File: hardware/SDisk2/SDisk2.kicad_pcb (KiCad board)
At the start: 2 copper layers, 29 parts, among them J1 SD_Card, J2 To Apple II DISK controller, SW1 BTN_UP, SW2 BTN_ENTER, SW3 BTN_DOWN, U1 74LS125, U2 ATmega328P-PU, U3 LM317_SOT-223, Y1 25Mhz

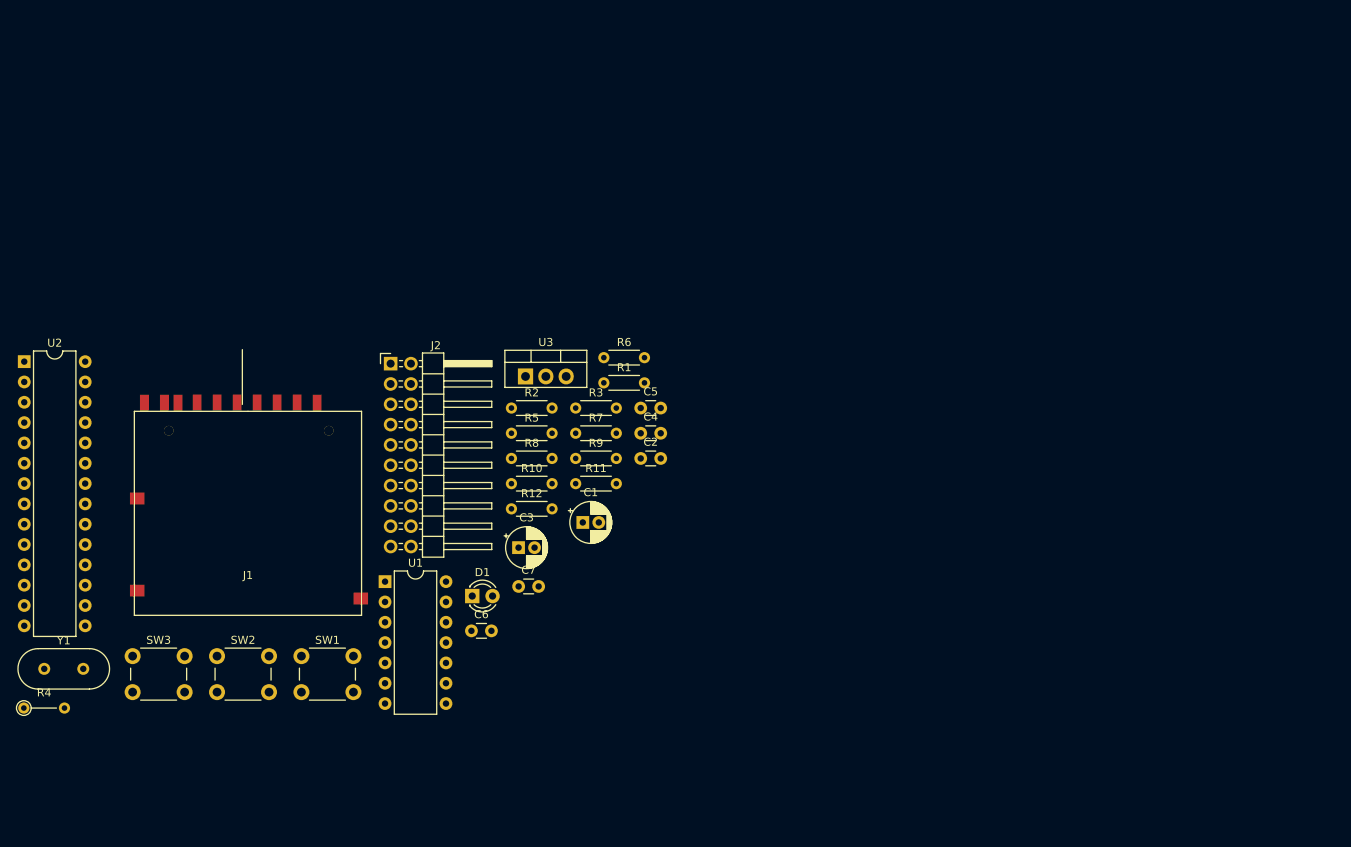
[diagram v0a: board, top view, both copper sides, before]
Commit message: Create netlist and begin place and route
Signed-off-by: Rangel Ivanov <rangelivanov88@gmail.com>
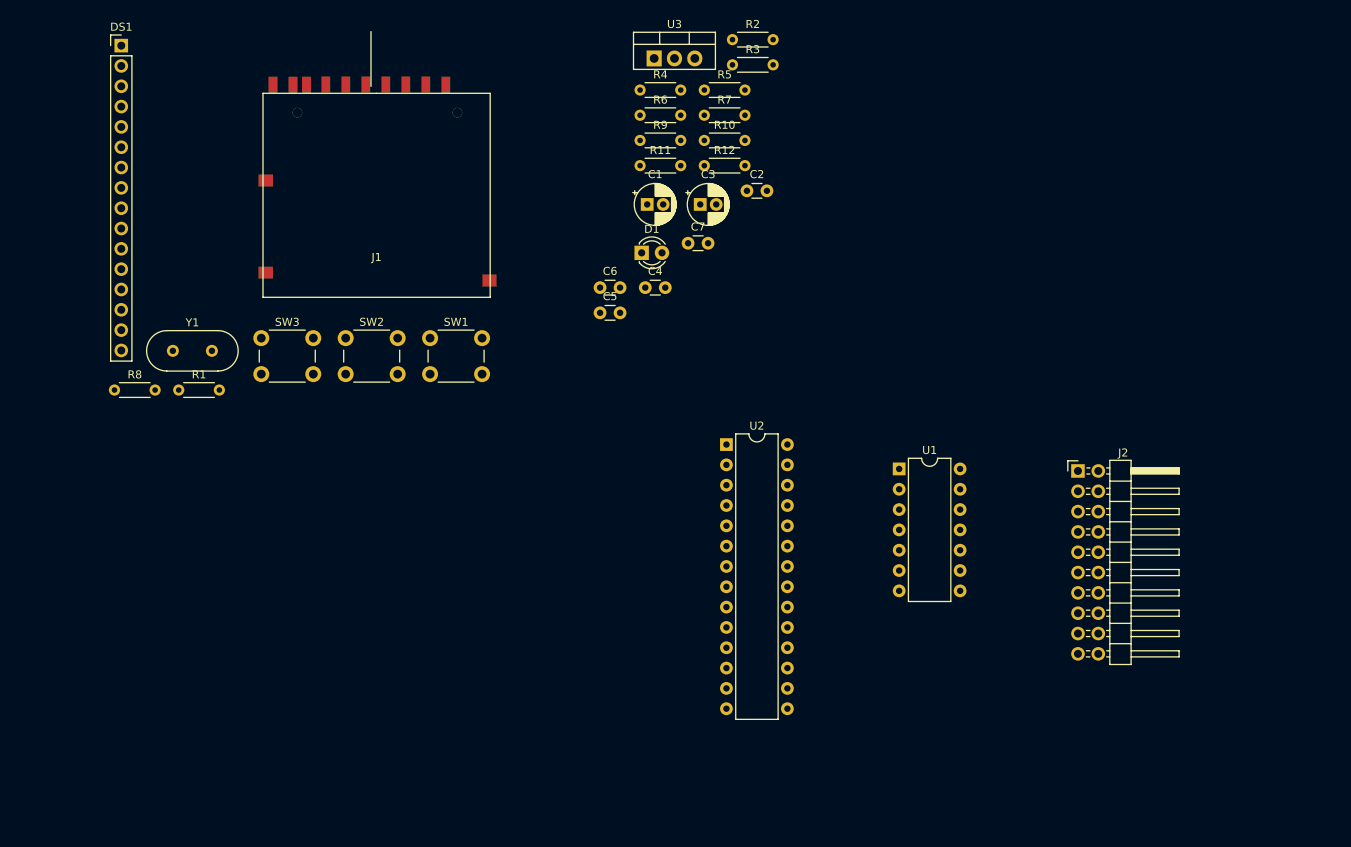
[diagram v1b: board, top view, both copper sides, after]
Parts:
- added DS1: WH1602B-TMI-CT#, Connector_PinHeader_2.54mm:PinHeader_1x16_P2.54mm_Vertical, F.Cu at (50.3, 41.1)
- R4: footprint Resistor_THT:R_Axial_DIN0204_L3.6mm_D1.6mm_P5.08mm_Vertical -> Resistor_THT:R_Axial_DIN0204_L3.6mm_D1.6mm_P5.08mm_Horizontal
- moved R4 109.1 mm to (115.2, 46.6)
- moved U2 88.4 mm to (126.0, 90.9)
- moved J2 87.0 mm to (169.9, 94.2)
- moved U1 65.8 mm to (147.6, 94.0)
- moved R2 53.7 mm to (126.7, 40.3)
- moved R1 53.1 mm to (57.5, 84.1)
- moved R8 50.4 mm to (49.5, 84.1)
- moved R10 49.2 mm to (123.2, 52.9)
- moved R12 49.2 mm to (123.2, 56.1)
- moved R5 49.2 mm to (123.2, 46.6)
- moved C3 48.5 mm to (122.7, 60.9)
- moved C7 47.8 mm to (121.2, 65.8)
- moved D1 47.8 mm to (115.4, 67.0)
- moved R3 47.2 mm to (126.7, 43.5)
- moved C6 45.8 mm to (110.2, 71.3)
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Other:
- net class Default: clearance 0.2 -> 0.22
- rule trace_clearance: 0.2 -> 0.22

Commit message: Initial PCB place and route
Signed-off-by: Rangel Ivanov <rangelivanov88@gmail.com>
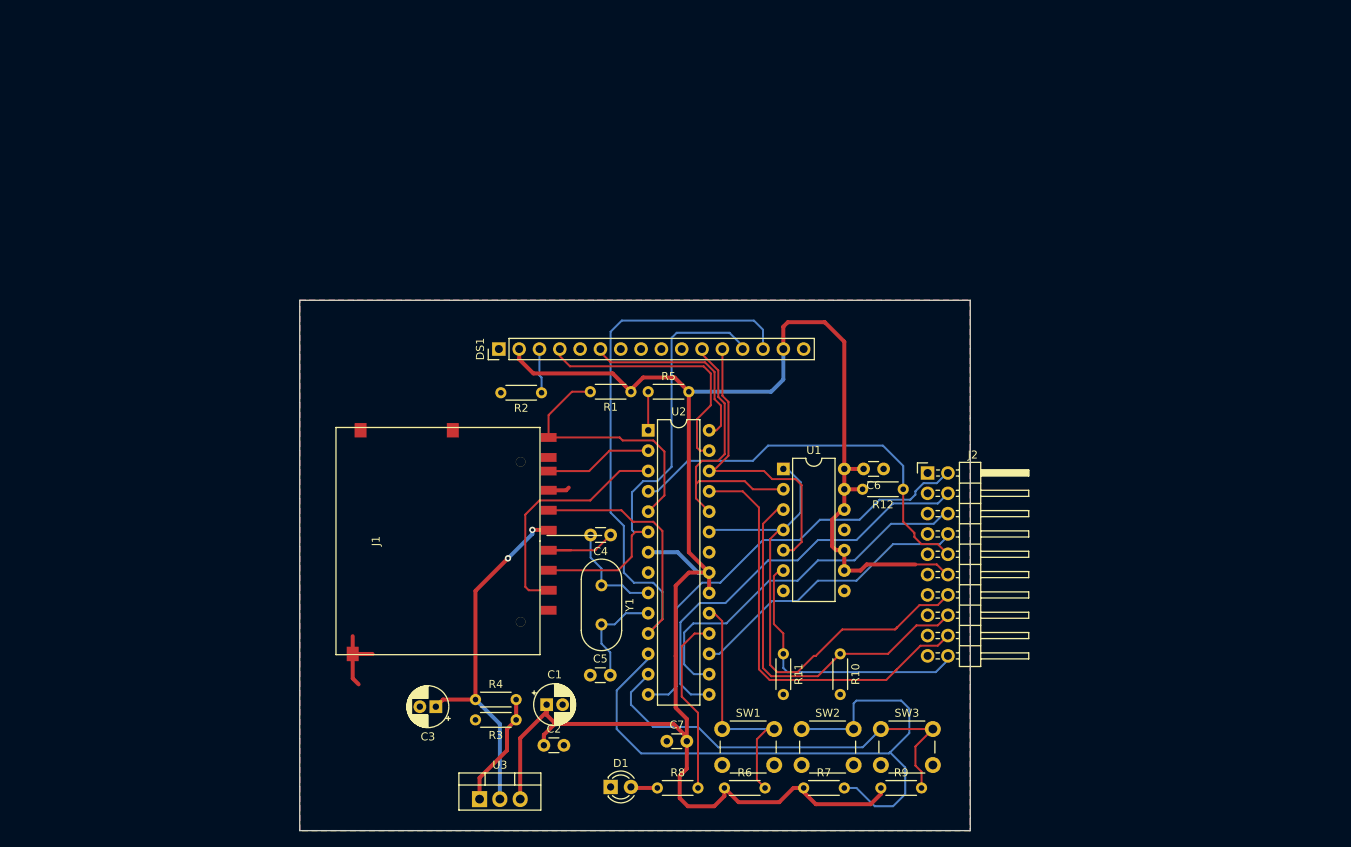
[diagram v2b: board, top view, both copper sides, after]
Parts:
- moved U3 95.1 mm to (95.1, 135.3)
- moved SW3 91.6 mm to (145.3, 126.5)
- moved R9 86.4 mm to (145.3, 133.9)
- moved R3 86.2 mm to (99.7, 125.3), turned to 180 degrees
- moved R7 85.0 mm to (135.6, 133.9)
- moved R6 84.7 mm to (125.7, 133.9)
- moved R8 84.1 mm to (117.3, 133.9)
- moved R4 78.9 mm to (94.6, 122.8)
- moved SW2 75.1 mm to (135.4, 126.5)
- moved C2 73.8 mm to (103.2, 128.5)
- moved C3 70.9 mm to (89.7, 123.7), turned to 180 degrees
- moved D1 66.9 mm to (111.5, 133.7)
- moved R10 66.4 mm to (140.2, 117.1), turned to 270 degrees
- moved C1 63.8 mm to (103.5, 123.4)
- moved R11 63.6 mm to (133.1, 117.1), turned to 270 degrees
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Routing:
- net +5V: track 0.00 -> 238.2 mm
- net /SD_CLK: track 0.00 -> 93.9 mm
- net /BTN_ENTER: track 0.00 -> 85.4 mm
- net /DRIVE_EN: track 0.00 -> 63.7 mm
- net /SD_DI: track 0.00 -> 55.5 mm
- net /STEP0: track 0.00 -> 54.9 mm
- net /BTN_DOWN: track 0.00 -> 54.2 mm
- net /WRITE: track 0.00 -> 54.0 mm
- net /STEP1: track 0.00 -> 52.0 mm
- net /W_REQUEST: track 0.00 -> 49.9 mm
- net /RD_PULSE: track 0.00 -> 48.4 mm
- net /STEP2: track 0.00 -> 46.7 mm
- net /3.3V: track 0.00 -> 45.2 mm, vias 0 -> 2
- net /LCD_D5: track 0.00 -> 39.0 mm
- net /LCD_D4: track 0.00 -> 36.3 mm
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- added copper zone on B.Cu, net (none)
- added copper zone on F.Cu, net GND
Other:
- board outline added: 83.8 x 66.3 mm

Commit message: WIP place and route
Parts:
- moved U1 17.6 mm to (130.4, 111.3), turned to 90 degrees
- moved C6 13.8 mm to (132.9, 99.4)
- moved R12 3.38 mm to (146.0, 93.9)
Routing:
- net /BTN_ENTER: track 85.4 -> 45.4 mm
- net /RD_PULSE: track 48.4 -> 23.2 mm
- net /DRIVE_EN: track 63.7 -> 40.7 mm
- net /STEP3: track 36.2 -> 44.3 mm
- net /LCD_D5: track 39.0 -> 46.6 mm
- net /LCD_D4: track 36.3 -> 41.9 mm
- net GND: track 22.8 -> 18.1 mm, vias 0 -> 6
- net /W_PROTECT: track 35.4 -> 31.9 mm
- net /BTN_DOWN: track 54.2 -> 51.0 mm
- net /STEP2: track 46.7 -> 49.7 mm
- net /W_REQUEST: track 49.9 -> 47.4 mm
- net /STEP0: track 54.9 -> 56.6 mm
- net /WRITE: track 54.0 -> 52.8 mm
- net /STEP1: track 52.0 -> 53.2 mm
- added copper zone on B.Cu, net GND
- removed copper zone on B.Cu, net (none)

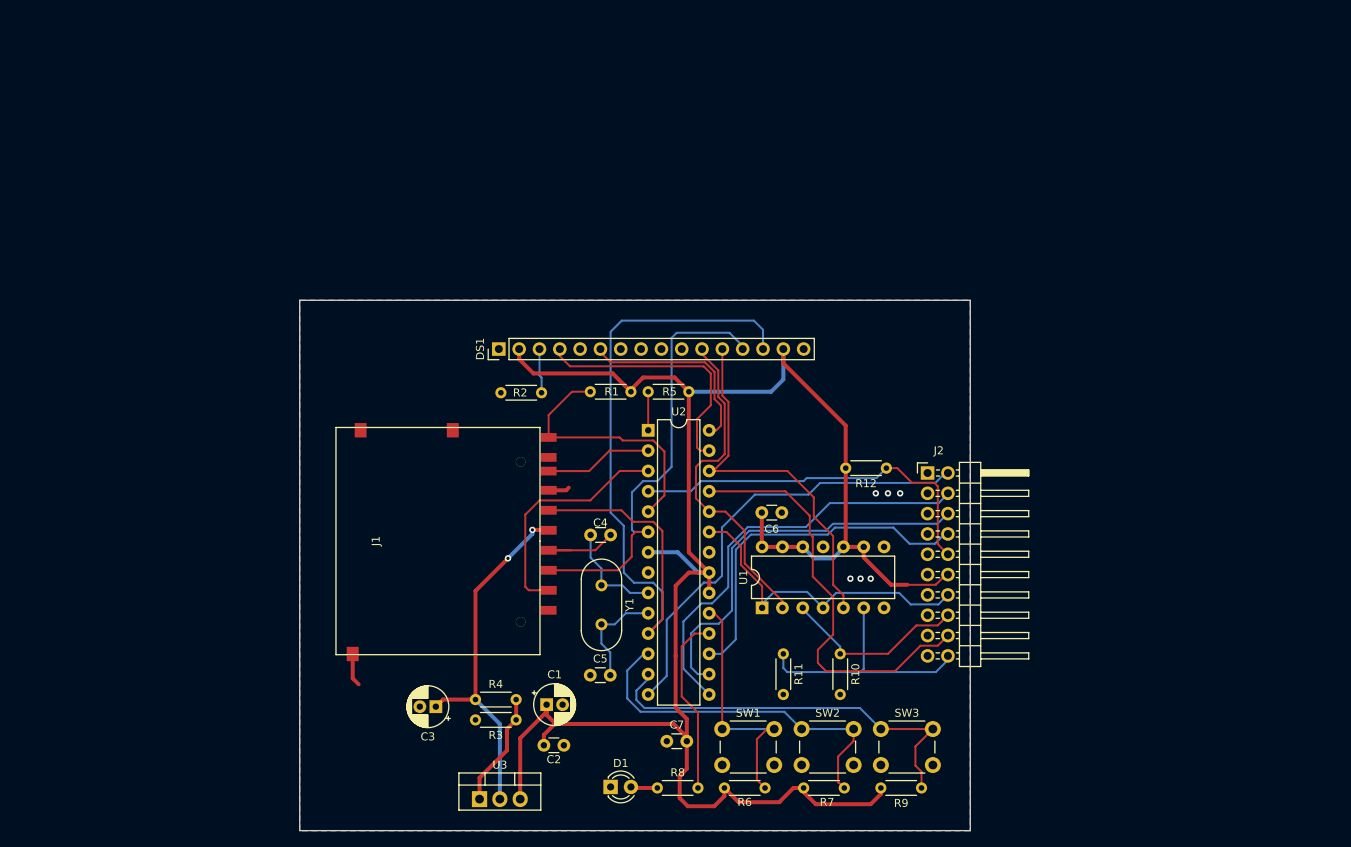
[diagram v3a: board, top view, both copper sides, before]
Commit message: Completely new place and route of PCB
Signed-off-by: Rangel Ivanov <rangelivanov88@gmail.com>
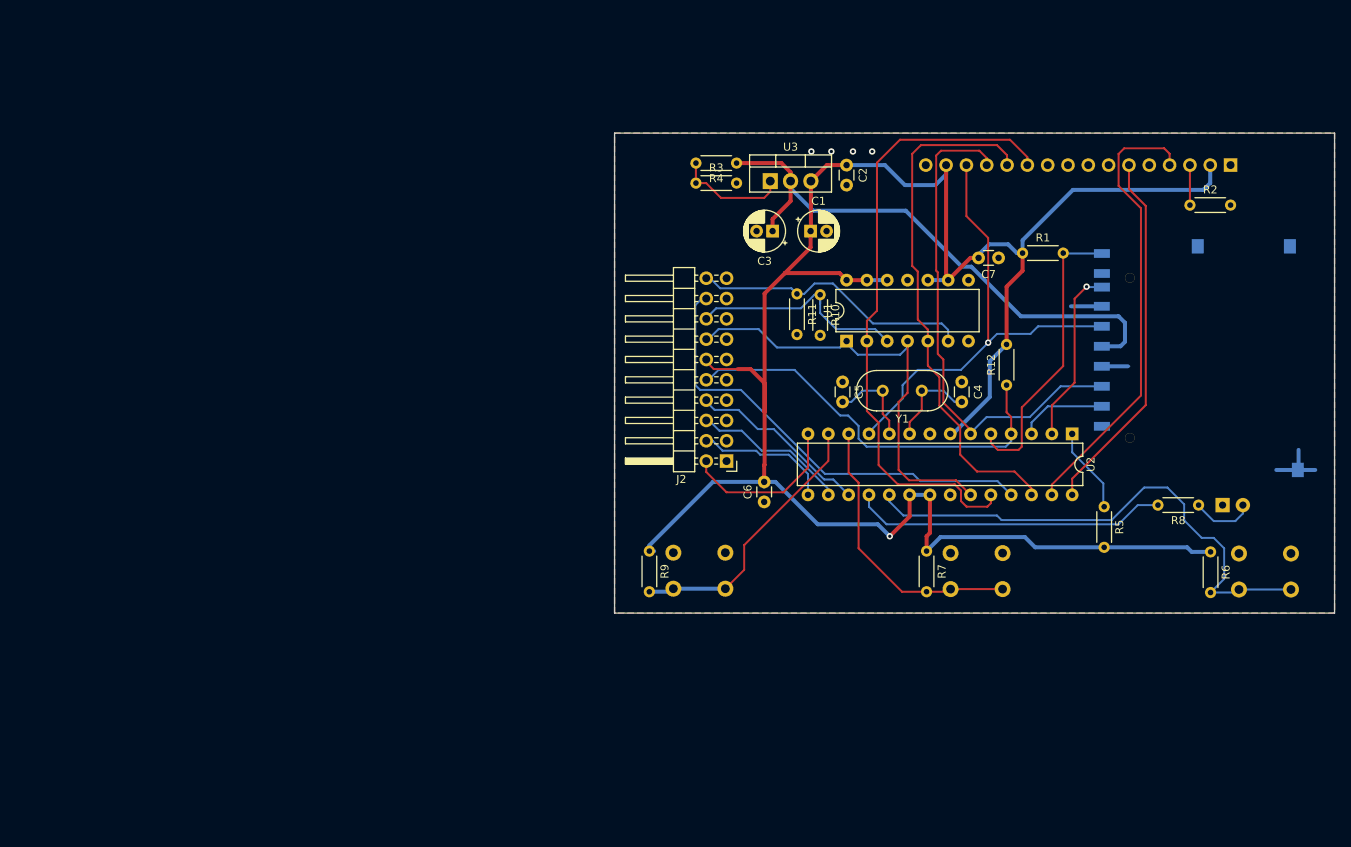
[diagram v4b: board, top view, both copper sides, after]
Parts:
- D1, DS1, J1, SW1, SW2, SW3: moved to B.Cu
- moved J1 113.7 mm to (194.0, 80.0)
- moved DS1 94.3 mm to (189.0, 56.0)
- moved U3 85.4 mm to (131.5, 58.0)
- moved R2 84.4 mm to (183.9, 61.0), turned to 0 degrees
- moved D1 84.2 mm to (188.0, 98.5)
- moved C2 81.8 mm to (141.0, 56.0), turned to 270 degrees
- moved R8 76.3 mm to (185.0, 98.5), turned to 180 degrees
- moved R4 74.6 mm to (127.2, 55.8), turned to 180 degrees
- moved C7 73.3 mm to (160.0, 67.6), turned to 180 degrees
- moved C3 72.8 mm to (131.8, 64.2)
- moved R3 70.8 mm to (122.2, 58.2), turned to 0 degrees
- moved C1 67.8 mm to (136.5, 64.2)
- moved R6 67.6 mm to (186.5, 104.3), turned to 270 degrees
- moved SW1 66.9 mm to (190.1, 109.0)
- moved R5 58.8 mm to (173.2, 98.7), turned to 270 degrees
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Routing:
- net /LCD_D4: track 41.9 -> 79.0 mm
- net /STEP1: track 53.2 -> 17.1 mm
- net /STEP0: track 56.6 -> 21.6 mm
- net /SD_CLK: track 93.9 -> 59.1 mm, vias 0 -> 1
- net /BTN_UP: track 31.7 -> 66.1 mm
- net /STEP2: track 49.7 -> 19.5 mm
- net +5V: track 238.0 -> 264.7 mm, vias 0 -> 1
- net /3.3V: track 45.2 -> 70.7 mm, vias 2 -> 0
- net /LCD_RS: track 33.1 -> 56.8 mm
- net /STEP3: track 44.3 -> 22.8 mm
- net /LCD_E: track 24.4 -> 45.9 mm
- net /LCD_D5: track 46.6 -> 65.6 mm
- net /SD_CS: track 29.8 -> 11.1 mm
- net Net-(R8-Pad2): track 22.6 -> 39.5 mm
- net /BTN_DOWN: track 51.0 -> 34.3 mm
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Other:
- board size 83.8 x 66.3 mm -> 90 x 60 mm

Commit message: Minor tweaks to PCB
Signed-off-by: Rangel Ivanov <rangelivanov88@gmail.com>
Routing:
- net GND: vias 4 -> 0

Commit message: Tidy up footprint references and values
Signed-off-by: Rangel Ivanov <rangelivanov88@gmail.com>
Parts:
- renumbered SW3 to DOWN, SW2 to ENTER, SW1 to UP
